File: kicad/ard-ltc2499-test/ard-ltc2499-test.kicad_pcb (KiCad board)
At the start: 2 copper layers, 122.3 x 71.1 mm, 40 parts, among them P1 Power, P2 Analog, P3 Digital, P4 Digital, P5 CONN_01X01, P6 CONN_01X01, P7 CONN_01X01, P8 CONN_01X01, U1 LT6654xxS6-1.25, U2 LT6654xxS6-2.5

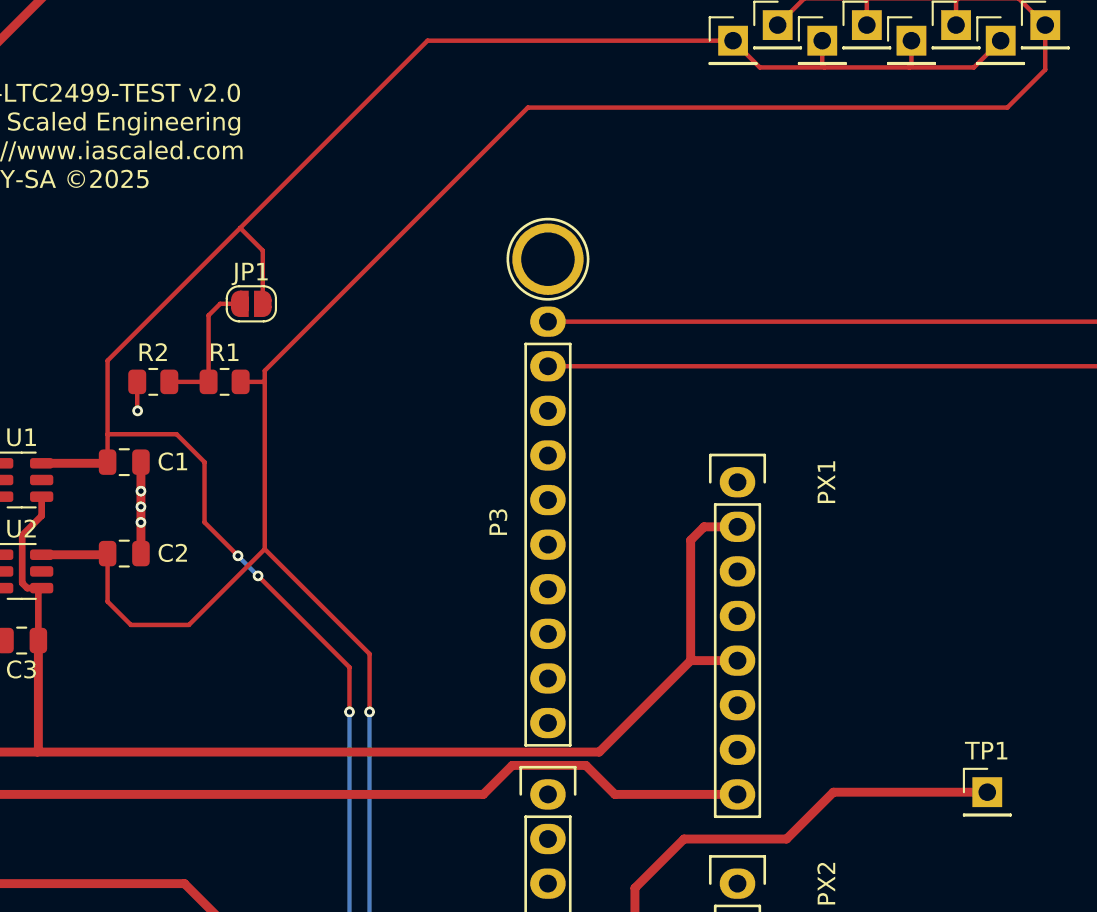
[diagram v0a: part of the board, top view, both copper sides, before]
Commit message: Added 5V divider and moved refernce divider to 1.25V
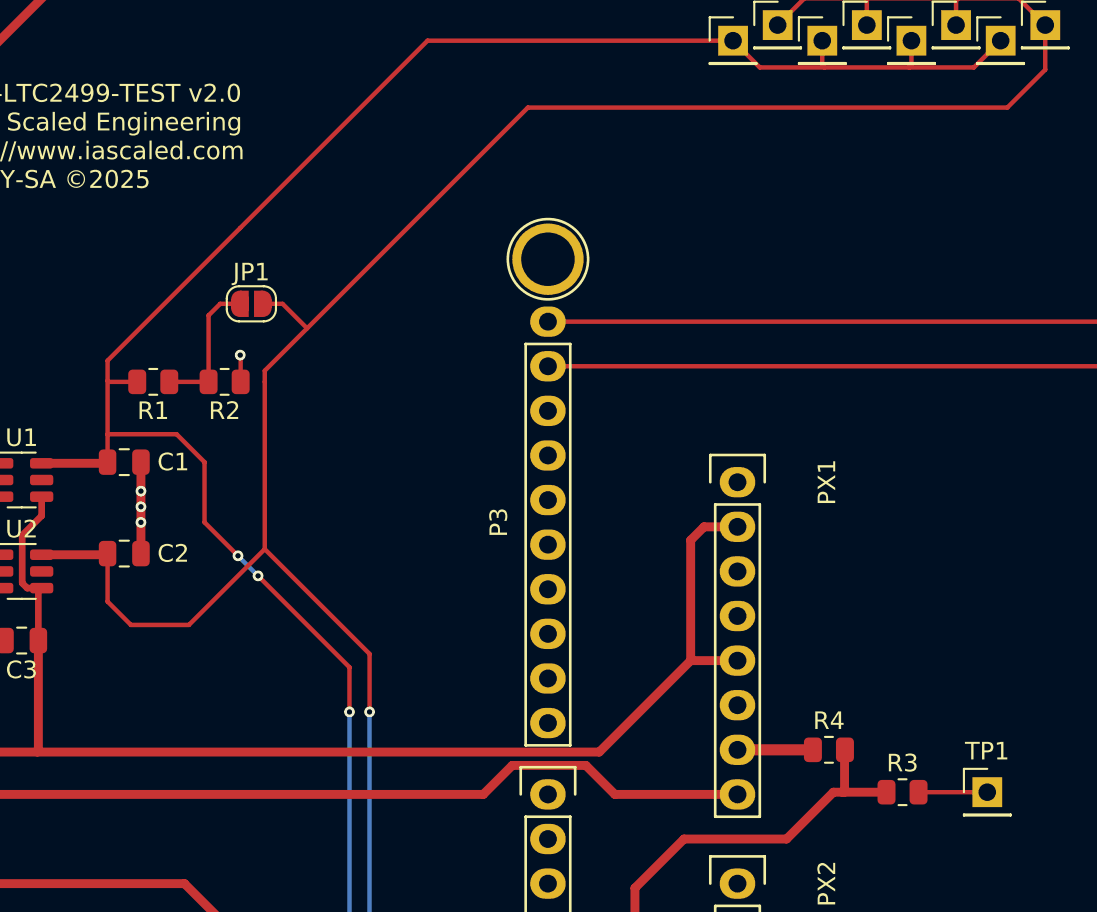
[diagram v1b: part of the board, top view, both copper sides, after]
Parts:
- added R3: 10k, Resistor_SMD:R_0805_2012Metric, F.Cu at (182.0, 103.4)
- added R4: 10k, Resistor_SMD:R_0805_2012Metric, F.Cu at (177.8, 101.0)
- moved R1 4.06 mm to (139.3, 80.0), turned to 180 degrees
- moved R2 4.06 mm to (143.4, 80.0), turned to 180 degrees
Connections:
- JP1 pad 2: /1p25V -> /2p5V
- R1 pad 2: /2p5V -> /1p25V
- TP1 pad 1: /A0 -> Net-(TP1-Pad1)
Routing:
- net GND: track 26.9 -> 31.0 mm
- net Net-(TP1-Pad1): track 0.00 -> 3.91 mm
- net /A0: track 96.5 -> 93.2 mm
- net /1p25V: track 179.9 -> 176.8 mm
- net /2p5V: track 195.9 -> 197.6 mm
